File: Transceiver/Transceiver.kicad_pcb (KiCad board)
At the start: 2 copper layers, 100 x 100 mm, 69 parts, among them J1 Conn_02x05, J2 Conn_02x20, J3 Conn_02x20, J4 Conn_02x05, J5 MountingHole, J6 MountingHole, J7 MountingHole, J8 MountingHole

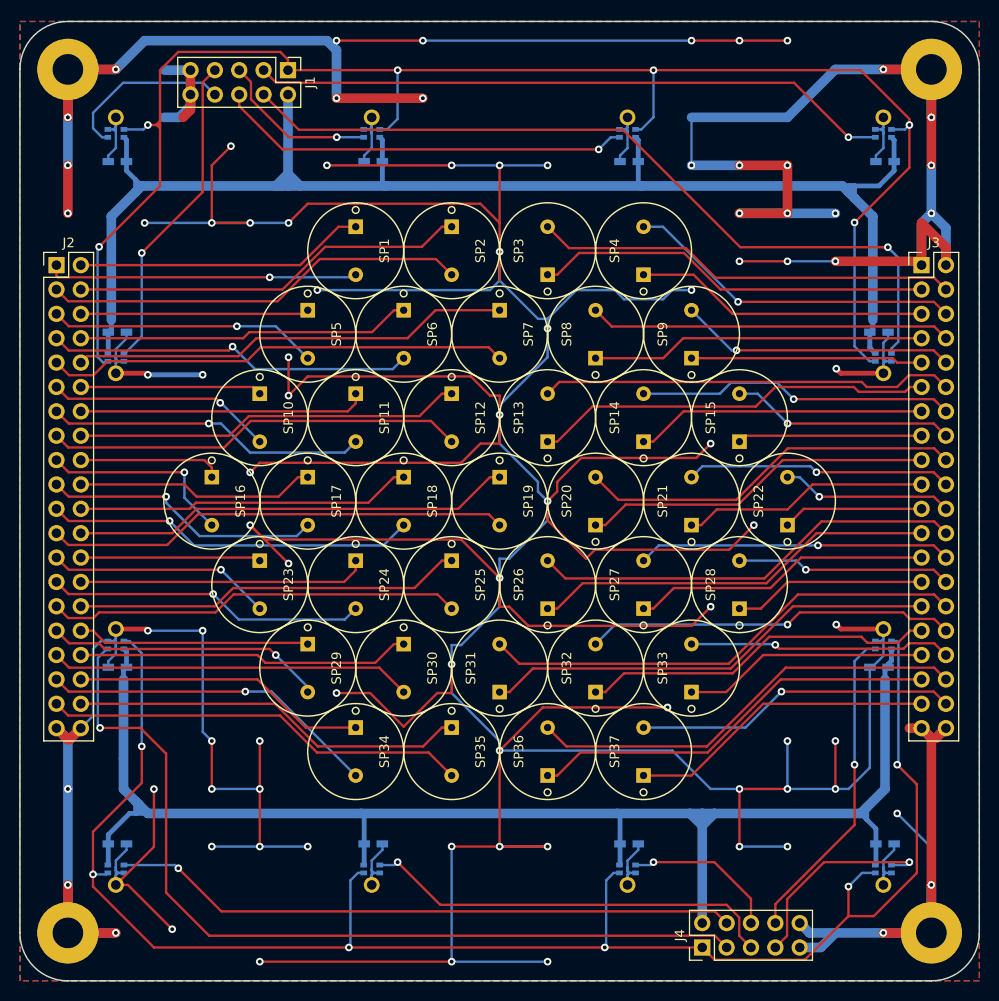
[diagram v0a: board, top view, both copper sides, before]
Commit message: トランシーバ基板にLEDとIMUを追加
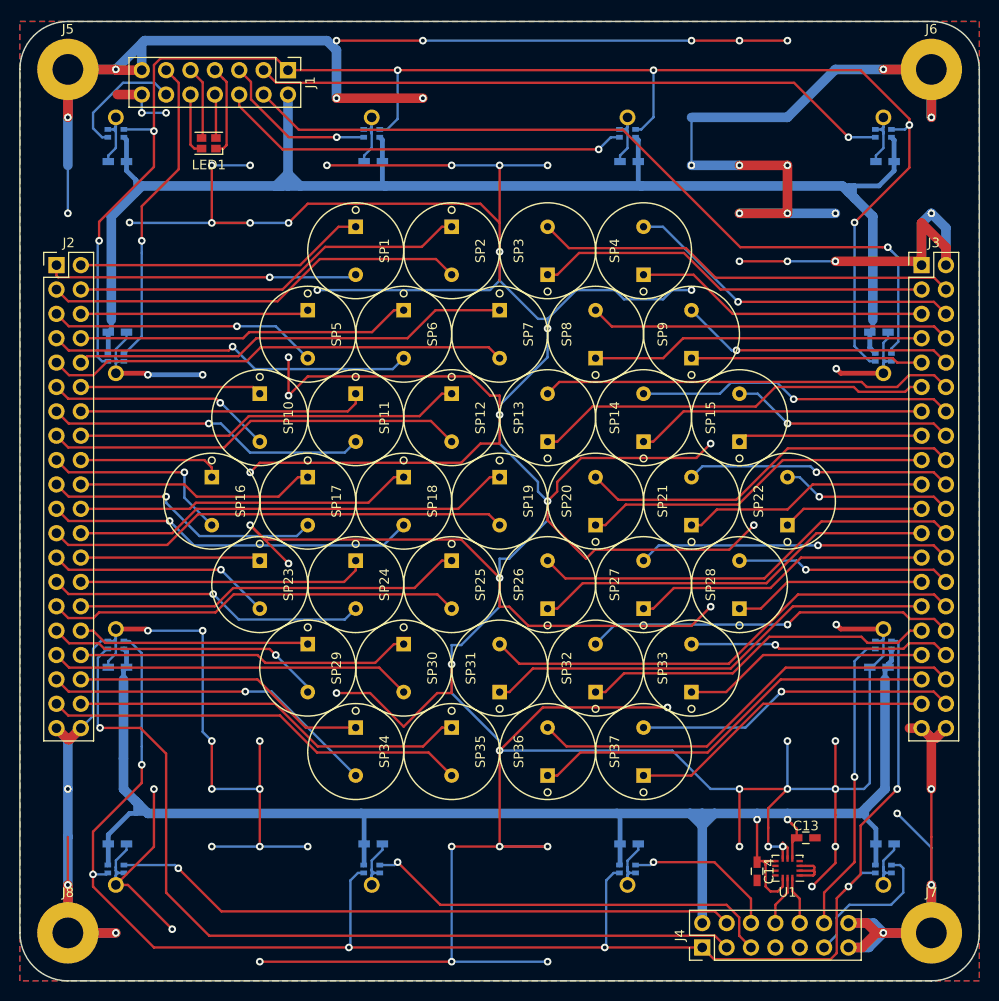
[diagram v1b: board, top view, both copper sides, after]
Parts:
- added C13: 0.1u, Capacitors_SMD:C_0603_HandSoldering, F.Cu at (161.9, 130.1)
- added C14: 0.1u, Capacitors_SMD:C_0603_HandSoldering, F.Cu at (156.8, 133.6)
- added LED1: RGB_LED, LEDs:LED_Cree-PLCC4_2x2mm_CW, F.Cu at (99.7, 57.7)
- added U1: LSM6DS3H, Housings_LGA:Bosch_LGA-14_3x2.5mm_Pitch0.5mm, F.Cu at (160.0, 133.3)
- J1, J4: value Conn_02x05 -> Conn_02x07; footprint Pin_Headers:Pin_Header_Straight_2x05_Pitch2.54mm -> Pin_Headers:Pin_Header_Straight_2x07_Pitch2.54mm
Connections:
- J1 pad 10: GND -> LED_B
- J1 pad 7: DATA12 -> LED_COM
- J1 pad 8: DATA1 -> LED_R
- J1 pad 9: GND -> LED_G
- J4 pad 10: GND -> IMU_SDA
- J4 pad 7: DATA7 -> GND
- J4 pad 8: DATA6 -> IMU_SCL
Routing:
- net GND: track 1080.9 -> 1106.1 mm, vias 86 -> 91
- net 3.3V_B: track 155.6 -> 174.6 mm, vias 0 -> 2
- net LED_COM: track 0.00 -> 9.58 mm
- net LED_G: track 0.00 -> 7.64 mm
- net LED_B: track 0.00 -> 6.55 mm
- net DATA7: track 21.9 -> 15.6 mm, vias 1 -> 0
- net IMU_SCL: track 0.00 -> 5.23 mm
- net DATA1: track 18.0 -> 13.0 mm
- net IMU_SDA: track 0.00 -> 5.02 mm
- net CLK_B: track 173.1 -> 168.3 mm
- net LED_R: track 0.00 -> 4.58 mm
- net CLK_A: track 167.2 -> 164.8 mm
- net DATA6: track 33.4 -> 31.3 mm
- net DATA12: track 33.5 -> 32.5 mm
